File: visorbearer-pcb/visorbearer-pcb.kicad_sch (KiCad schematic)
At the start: 79 parts, among them U1 XIAO nRF52840 Plus, U3 LP5012, U5 LP5012

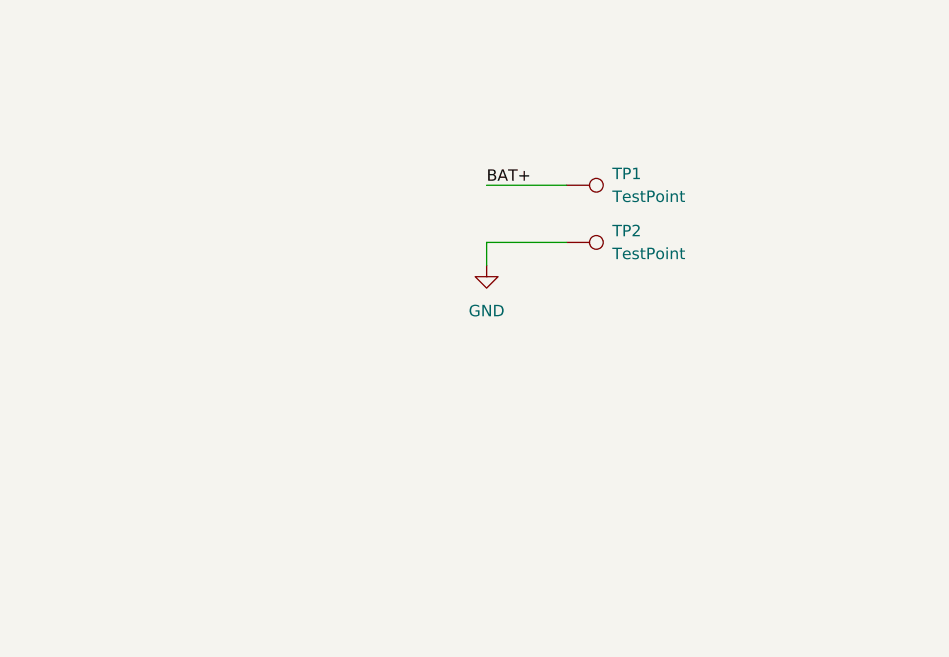
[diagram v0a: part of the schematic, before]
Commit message: pcb: change to hand-solderable diode footprint, move battery pads, add LP5012 EN test points
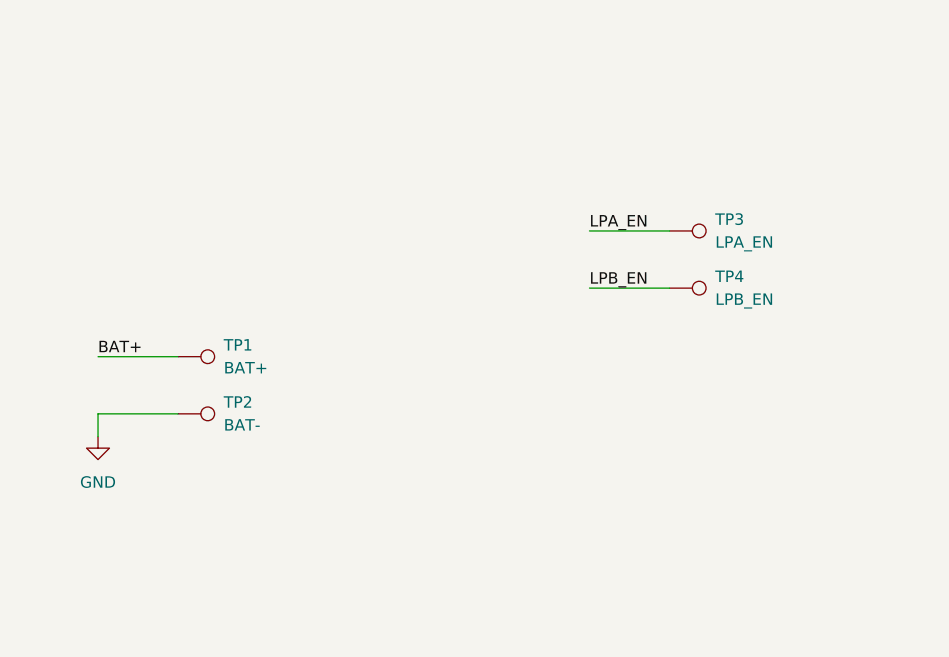
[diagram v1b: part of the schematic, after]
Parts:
- added TP3: LPA_EN, TestPoint:TestPoint_Pad_D1.5mm, symbol Connector:TestPoint
- added TP4: LPB_EN, TestPoint:TestPoint_Pad_D1.5mm, symbol Connector:TestPoint
- D1, D10, D11, D12, D13, D14, D15, D16, D2, D3, D4, D5, D6, D7, D8, D9: footprint Package_TO_SOT_SMD:SOT-23 -> Package_TO_SOT_SMD:SOT-23_Handsoldering
- TP1: value TestPoint -> BAT+
- TP2: value TestPoint -> BAT-
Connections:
- net LPA_EN: now also TP3.1
- net LPB_EN: now also TP4.1
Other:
- moved on the sheet: TP1, TP2
